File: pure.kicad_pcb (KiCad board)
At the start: 2 copper layers, 50 x 60 mm, 69 parts, among them J1 TX, J10 AudioJack3_Ground_SwitchTR, J2 AudioJack3_Ground_SwitchTR, J6 RX, K3 FRT5_separated, Q9 MMBT2222A, U1 78M09, U10 MC33079, U5 MC33079

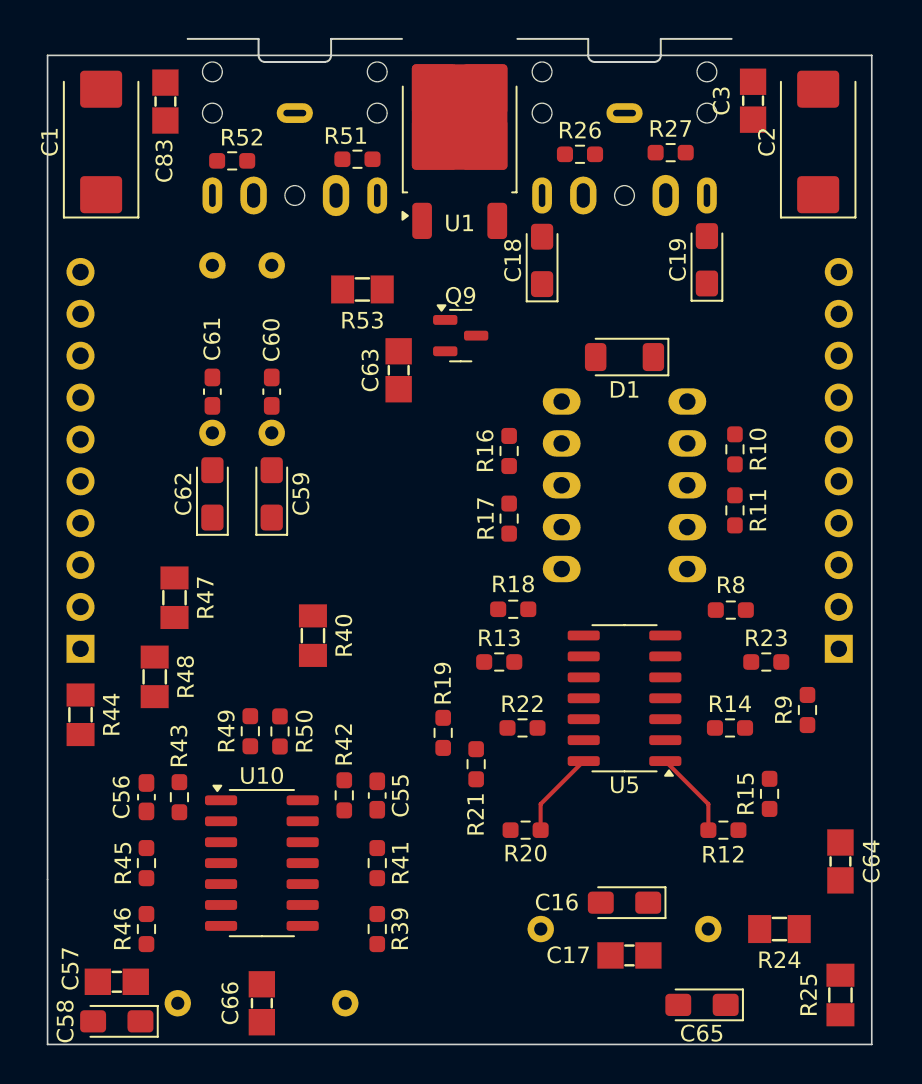
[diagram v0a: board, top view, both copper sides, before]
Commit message: add whole module PCB
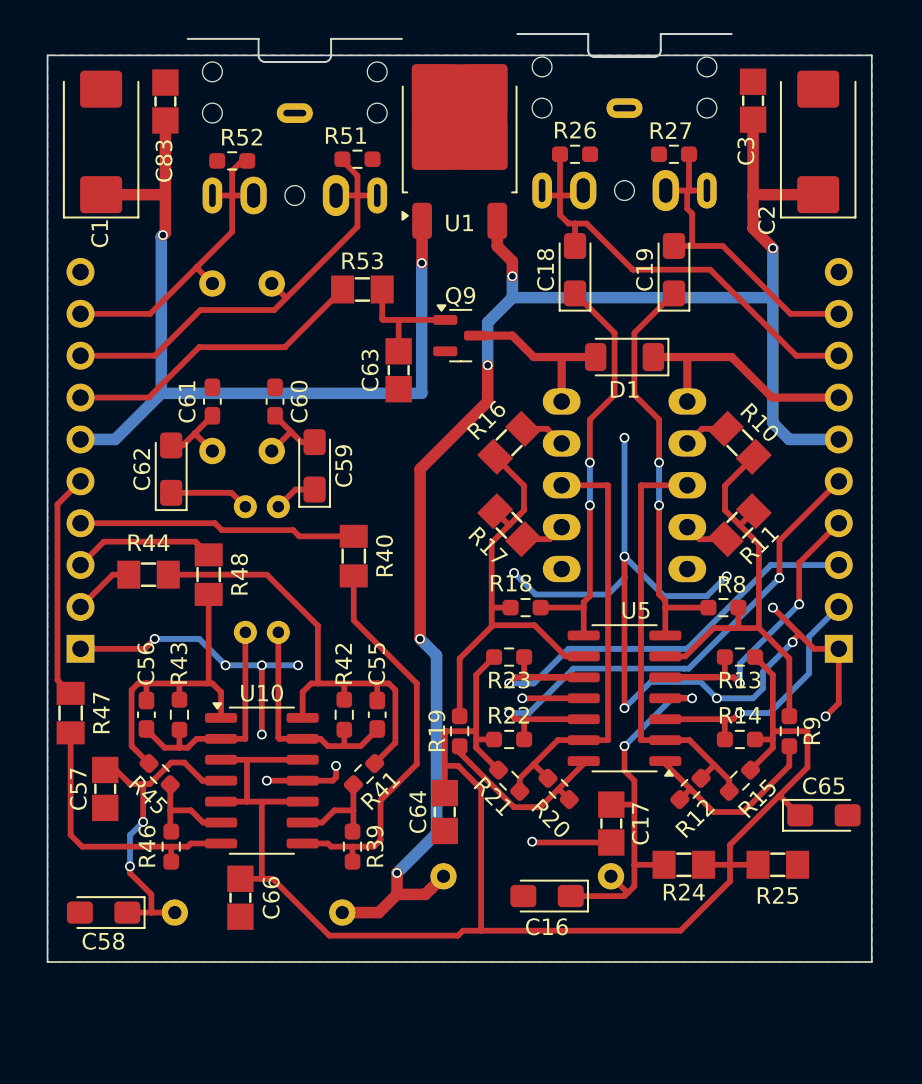
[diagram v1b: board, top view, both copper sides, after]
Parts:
- R10, R11, R16, R17: footprint Resistor_SMD:R_0603_1608Metric_Pad0.98x0.95mm_HandSolder -> SDR_footprints:R_1206_0603
- R49, R50: footprint Resistor_SMD:R_0603_1608Metric_Pad0.98x0.95mm_HandSolder -> Resistor_THT:R_Axial_DIN0204_L3.6mm_D1.6mm_P7.62mm_Horizontal; moved to B.Cu
- moved C64 24.2 mm to (124.1, 85.9), turned to 90 degrees
- moved R23 15.6 mm to (128.0, 76.5), turned to 180 degrees
- moved R13 14.6 mm to (142.0, 76.5), turned to 180 degrees
- moved C65 13.7 mm to (147.1, 86.1), turned to 0 degrees
- moved C57 11.7 mm to (103.5, 84.5), turned to -90 degrees
- moved R44 9.45 mm to (106.1, 71.5), turned to 0 degrees
- moved R47 9.42 mm to (101.4, 79.9)
- moved R25 8.77 mm to (144.3, 89.1), turned to 180 degrees
- moved C17 8.08 mm to (134.2, 86.6), turned to 90 degrees
- moved R48 7.01 mm to (109.8, 71.5)
- moved R24 6.99 mm to (138.6, 89.1)
- moved L4 6.71 mm to (124.0, 89.8)
- moved C58 6.65 mm to (103.4, 92.0)
- moved C66 6.53 mm to (111.7, 91.1)
- moved R50 6.01 mm to (114.0, 75.0)
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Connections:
- D1 pad 1: +12V -> RELAY_POWER
- J6 pad 7: unconnected-(J6-Pin_7-Pad7) -> RELAY_POWER
- K3 pad 1: +12V -> RELAY_POWER
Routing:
- net +5V: track 0.00 -> 102.7 mm
- net +10V: track 0.00 -> 95.1 mm, vias 0 -> 5
- net GND: track 0.00 -> 88.3 mm, vias 0 -> 18
- net +12V: track 0.00 -> 52.9 mm, vias 0 -> 2
- net RX90: track 0.00 -> 35.2 mm, vias 0 -> 1
- net RX270: track 0.00 -> 33.1 mm, vias 0 -> 2
- net Net-(C55-Pad1): track 0.00 -> 28.4 mm
- net TX_IQ_Q: track 0.00 -> 28.3 mm
- net I_LINE_IN: track 0.00 -> 28.0 mm
- net Net-(U5B--): track 0.00 -> 26.9 mm
- net Net-(U5C--): track 0.00 -> 26.8 mm
- net Net-(U5D--): track 0.00 -> 26.6 mm
- net Net-(U5A--): track 0.00 -> 26.5 mm
- net R_LINE_IN: track 0.00 -> 25.1 mm, vias 0 -> 2
- net L_LINE_IN: track 0.00 -> 25.1 mm, vias 0 -> 2
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- added copper zone on B.Cu, net GND
- added copper zone on F.Cu, net GND
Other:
- board size 50 x 60 mm -> 50 x 55 mm
- board text added: "+10V"
- board text added: "+12V"
- board text added: "GND"
- board text added: "IF_PRE"
- board text added: "I_LineIN"
- board text added: "I_Out"
- board text added: "Q_LineIN"
- board text added: "Q_Out"
- board text added: "REL_POW"
- board text added: "RX0"
- board text added: "RX180"
- board text added: "RX270"
- board text added: "RX90"
- board text added: "TX0"
- board text added: "TX180"
- board text added: "TX270"
- board text added: "TX90"
